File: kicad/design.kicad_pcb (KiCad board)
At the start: 2 copper layers, 99.1 x 99.1 mm, 55 parts, among them P1 CONN_10, P2 CONN_10, SW1 SW_00, SW10 SW_10, SW11 SW_21, SW12 SW_22, SW13 SW_23, SW14 SW_24, SW15 SW_20, SW16 SW_31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

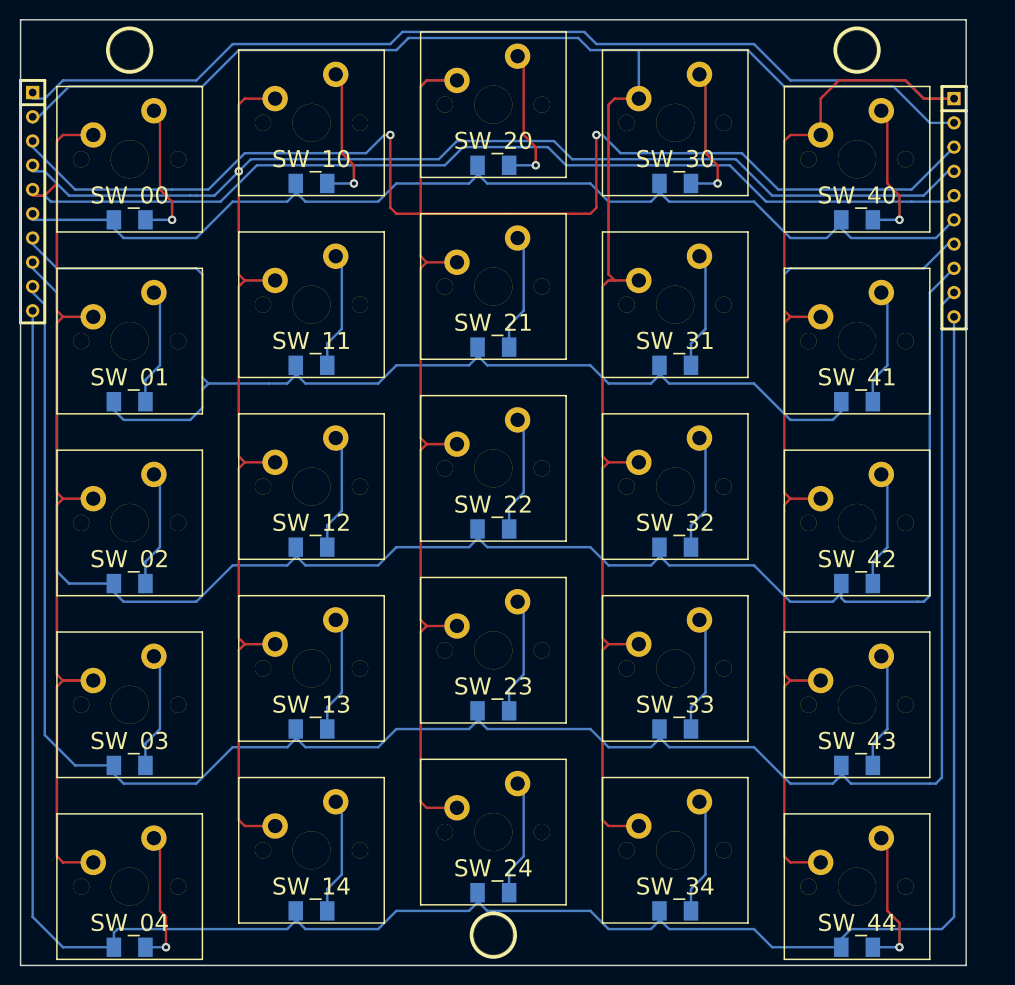
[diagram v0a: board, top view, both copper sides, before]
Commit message: added ground planes
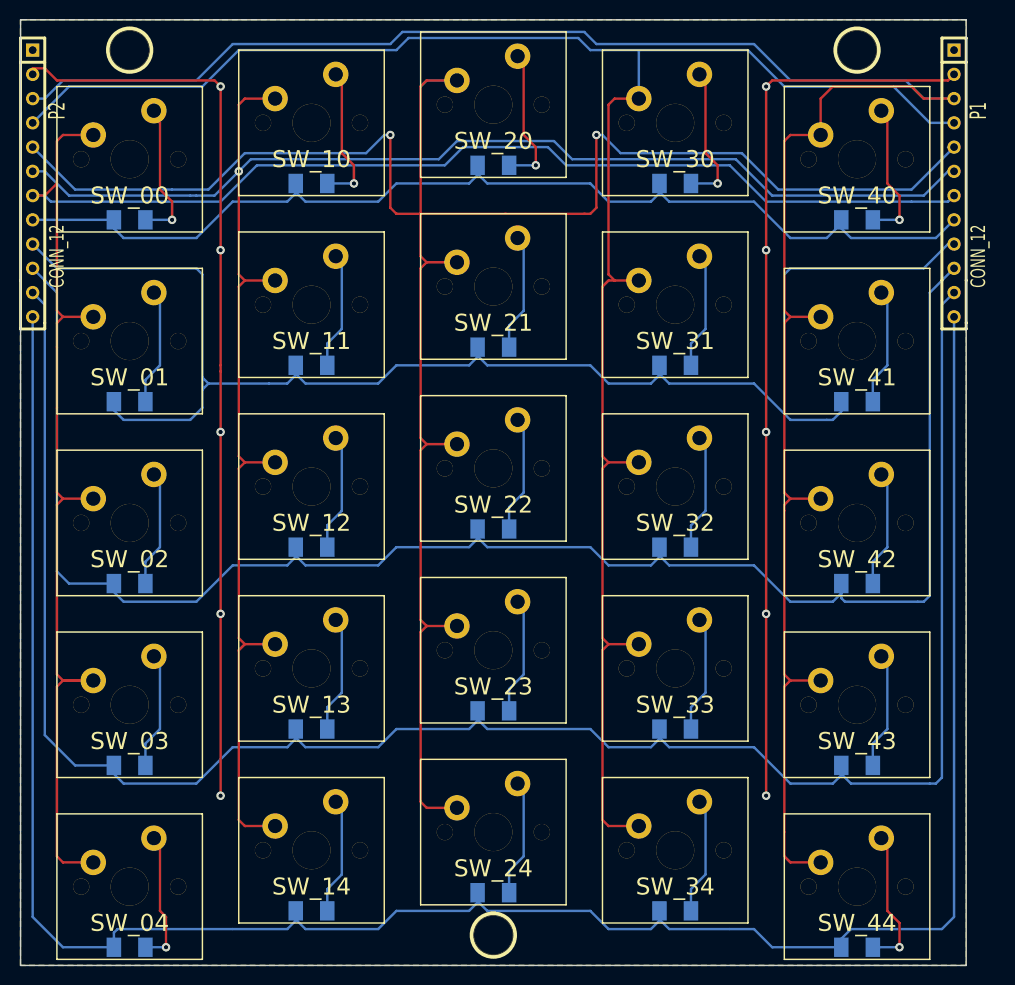
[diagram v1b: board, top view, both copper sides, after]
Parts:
- P1, P2: value CONN_10 -> CONN_12; footprint SIL-10 -> SIL-12
- moved P1 2.54 mm to (123.2, 42.5)
- moved P2 1.91 mm to (26.7, 42.5)
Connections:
- P1 pad 1: C4 -> GND
- P1 pad 10: R4 -> R2
- P1 pad 2: C3 -> GND
- P1 pad 3: N-0000027 -> C4
- P1 pad 4: C1 -> C3
- P1 pad 5: C0 -> N-0000022
- P1 pad 6: R0 -> C1
- P1 pad 7: R1 -> C0
- P1 pad 8: R2 -> R0
- P1 pad 9: R3 -> R1
- P2 pad 1: C4 -> GND
- P2 pad 10: R4 -> R2
- P2 pad 2: C3 -> GND
- P2 pad 3: N-0000027 -> C4
- P2 pad 4: C1 -> C3
- P2 pad 5: C0 -> N-0000022
- P2 pad 6: R0 -> C1
- P2 pad 7: R1 -> C0
- P2 pad 8: R2 -> R0
- P2 pad 9: R3 -> R1
- SW11 pad 2: N-0000027 -> N-0000022
- SW12 pad 2: N-0000027 -> N-0000022
- SW13 pad 2: N-0000027 -> N-0000022
- SW14 pad 2: N-0000027 -> N-0000022
- SW15 pad 2: N-0000027 -> N-0000022
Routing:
- net N-0000027: track 219.6 -> 0.00 mm, vias 2 -> 0
- net N-0000022: track 0.00 -> 219.6 mm, vias 0 -> 2
- net GND: track 0.00 -> 189.3 mm, vias 0 -> 10
- net C4: track 215.8 -> 215.3 mm
- added copper zone on B.Cu, net GND
- added copper zone on F.Cu, net GND
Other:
- rule via_min_drill: 0.3048 -> 0.50038
- rule via_min_size: 0.889 -> 0.7493
